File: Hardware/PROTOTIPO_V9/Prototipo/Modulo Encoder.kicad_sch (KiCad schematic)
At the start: 0 parts

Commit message: Esquematico Encoder
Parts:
- added U7: KY-040, KY-040:KY-040-PORT, symbol KY-040:KY-040
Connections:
- new net +5V: U7.VCC
- new net ENC_CLK: U7.CLK
- new net ENC_DT: U7.DT
- new net ENC_SW: U7.SW
- new net GND: U7.GND

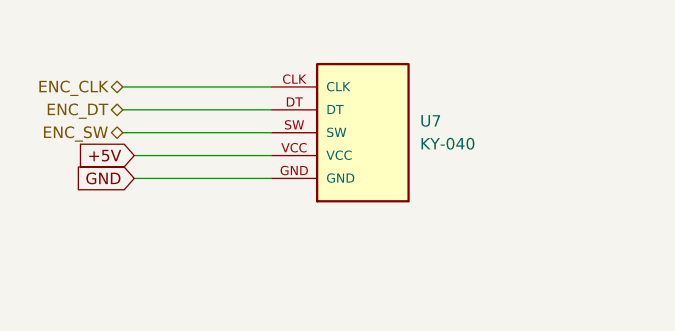
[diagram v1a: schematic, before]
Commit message: Se agrega sch/fp W5500, ILI9341 y fp BluePill
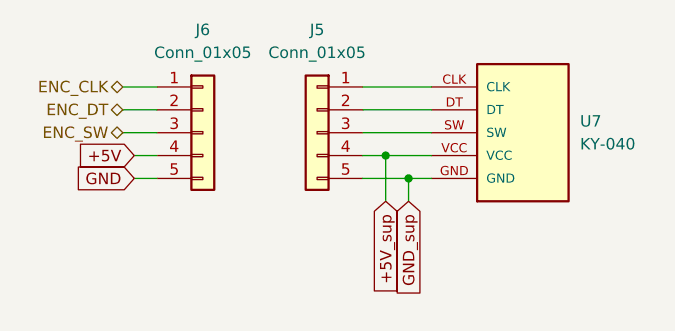
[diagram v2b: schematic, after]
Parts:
- added J5, J6: Conn_01x05, symbol Connector_Generic:Conn_01x05
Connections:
- net +5V: now also J6.4 (Pin_4); no longer U7.VCC
- net ENC_CLK: now also J6.1 (Pin_1); no longer U7.CLK
- net ENC_DT: now also J6.2 (Pin_2); no longer U7.DT
- net ENC_SW: now also J6.3 (Pin_3); no longer U7.SW
- net GND: now also J6.5 (Pin_5); no longer U7.GND
- new net: J5.1 (Pin_1), U7.CLK
- new net: J5.2 (Pin_2), U7.DT
- new net: J5.3 (Pin_3), U7.SW
- new net +5V_sup: J5.4 (Pin_4), U7.VCC
- new net GND_sup: J5.5 (Pin_5), U7.GND
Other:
- moved on the sheet: U7

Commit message: Bus de salida
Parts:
- removed J5, J6: Conn_01x05, symbol Connector_Generic:Conn_01x05
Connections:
- net ENC_CLK: now also U7.CLK
- net ENC_DT: now also U7.DT
- net ENC_SW: now also U7.SW
- net +5V_sup renamed ENC_+5V
- net GND_sup renamed ENC_GND

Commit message: Asignación de huellas
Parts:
- U7: footprint KY-040:KY-040-PORT -> Connector_PinSocket_2.54mm:PinSocket_1x05_P2.54mm_Vertical
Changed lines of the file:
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@@
 			)
 		)
-		(property "Footprint" "KY-040:KY-040-PORT"
+		(property "Footprint" "Connector_PinSocket_2.54mm:PinSocket_1x05_P2.54mm_Vertical"
 			(at 179.07 67.31 0)
 			(effects

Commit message: fp definitivos - Planteo de PCB con componentes
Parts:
- U7: footprint Connector_PinSocket_2.54mm:PinSocket_1x05_P2.54mm_Vertical -> footprints_proyecto:MODULE_KY-040
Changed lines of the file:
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@@
 			)
 		)
-		(property "Footprint" "Connector_PinSocket_2.54mm:PinSocket_1x05_P2.54mm_Vertical"
+		(property "Footprint" "footprints_proyecto:MODULE_KY-040"
 			(at 179.07 67.31 0)
 			(effects
